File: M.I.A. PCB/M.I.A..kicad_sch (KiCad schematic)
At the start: 44 parts, among them J1 USB_C_Receptacle_USB2.0_16P, SW1 SW_Push, SW2 SW_Push, U1 W25Q128JVS, U2 RP2350B-QFN80, Y1 ABM8-272-T3

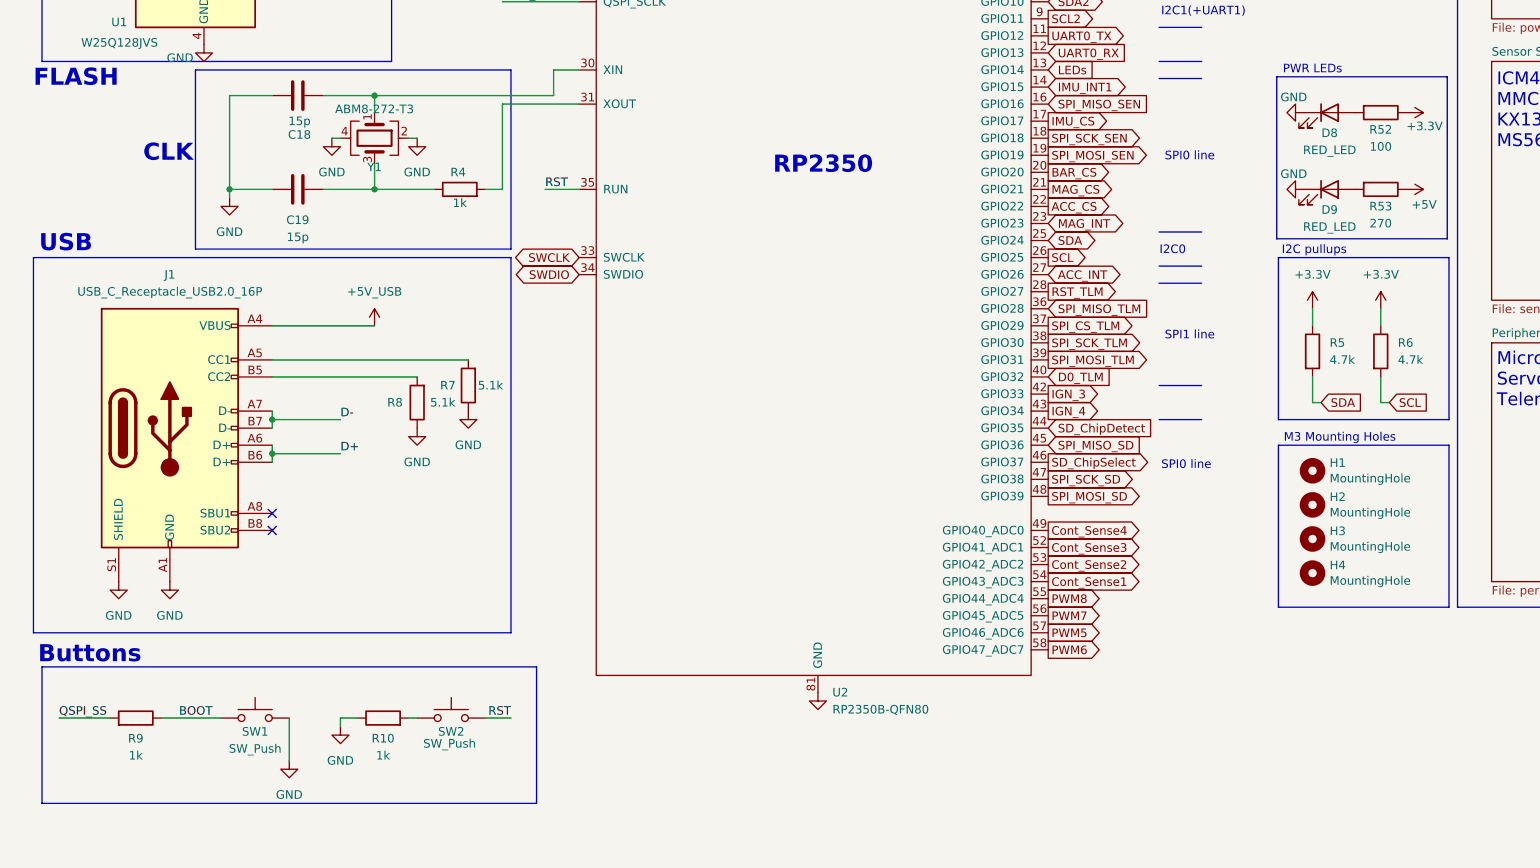
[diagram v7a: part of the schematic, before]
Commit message: Updated top connectors to be TLM_SPI
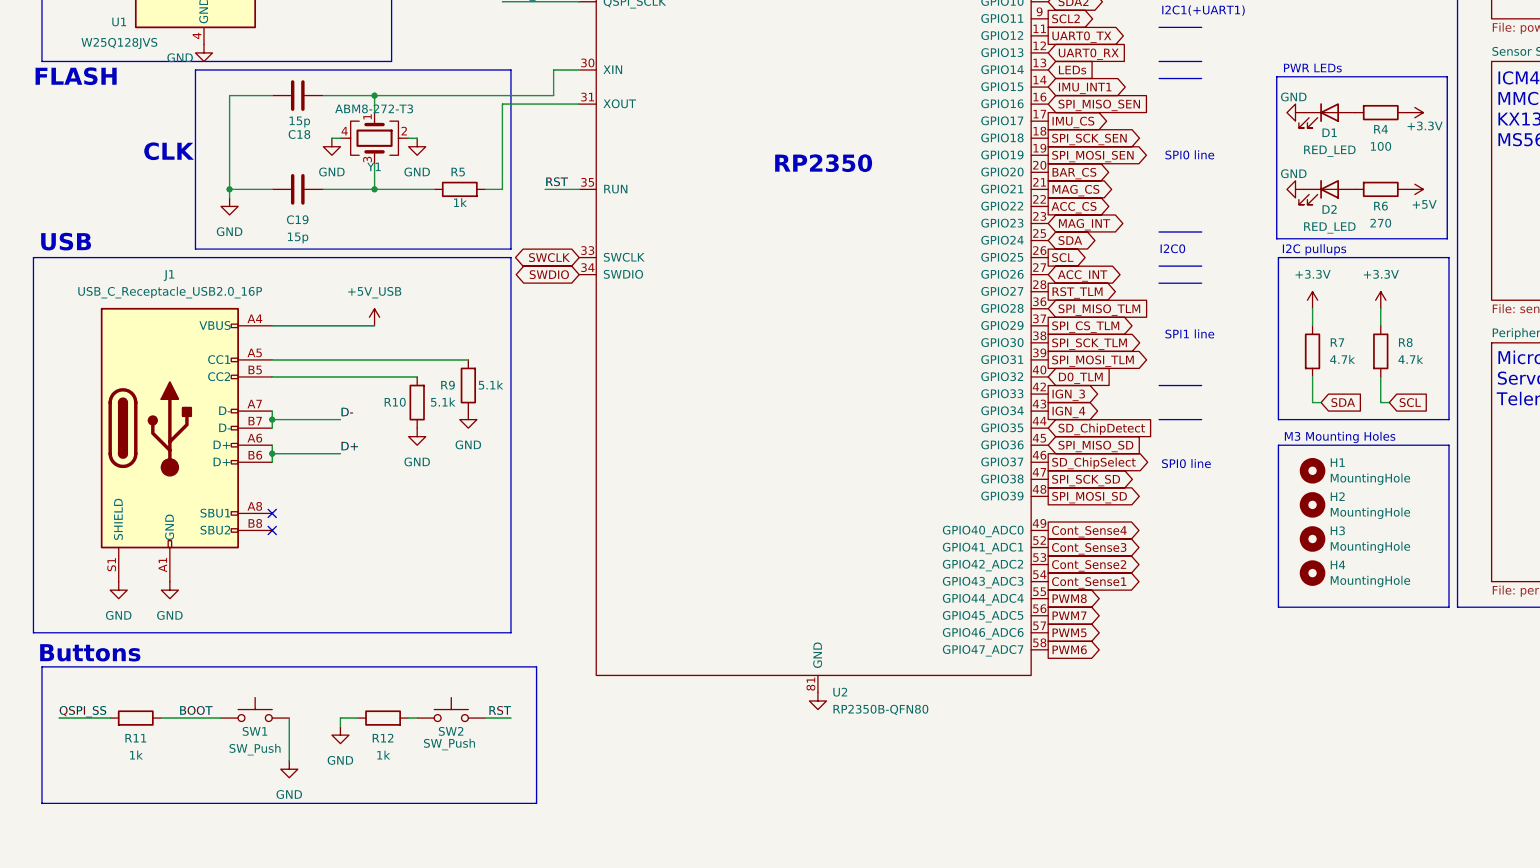
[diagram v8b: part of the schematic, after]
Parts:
- renumbered D8 to D1, D9 to D2, R8 to R10, R9 to R11, R10 to R12, R52 to R4, R4 to R5, R53 to R6, R5 to R7, R6 to R8, R7 to R9
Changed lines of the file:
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@@
 		(on_board yes)
 		(dnp no)
-		(property "Reference" "#PWR0175"
+		(property "Reference" "#PWR015"
 			(at 215.9 91.44 0)
 			(effects
@@
 			(project "M.I.A."
 				(path "/4d55825e-4251-44bf-9376-9abd9228f348"
-					(reference "#PWR0175")
+					(reference "#PWR015")
 					(unit 1)
 				)
@@
 		(dnp no)
 		(fields_autoplaced yes)
-		(property "Reference" "#PWR015"
+		(property "Reference" "#PWR017"
 			(at 72.39 101.6 0)
 			(effects
@@
 			(project "M.I.A."
 				(path "/4d55825e-4251-44bf-9376-9abd9228f348"
-					(reference "#PWR015")
+					(reference "#PWR017")
 					(unit 1)
 				)
@@
 		(on_board yes)
 		(dnp no)
-		(property "Reference" "R52"
+		(property "Reference" "R4"
 			(at 215.9 93.98 90)
 			(effects
@@
 			(project "M.I.A."
 				(path "/4d55825e-4251-44bf-9376-9abd9228f348"
-					(reference "R52")
+					(reference "R4")
 					(unit 1)
 				)
@@
 		(on_board yes)
 		(dnp no)
-		(property "Reference" "R4"
+		(property "Reference" "R5"
 			(at 78.486 100.33 90)
 			(effects
@@
 			(project "M.I.A."
 				(path "/4d55825e-4251-44bf-9376-9abd9228f348"
-					(reference "R4")
+					(reference "R5")
 					(unit 1)
 				)
@@
 		(on_board yes)
 		(dnp no)
-		(property "Reference" "D8"
+		(property "Reference" "D1"
 			(at 208.28 94.488 0)
 			(effects
@@
 			(project "M.I.A."
 				(path "/4d55825e-4251-44bf-9376-9abd9228f348"
-					(reference "D8")
+					(reference "D1")
 					(unit 1)
 				)
@@
 		(dnp no)
 		(fields_autoplaced yes)
-		(property "Reference" "#PWR025"
+		(property "Reference" "#PWR030"
 			(at 53.34 194.31 0)
 			(effects
@@
 			(project "M.I.A."
 				(path "/4d55825e-4251-44bf-9376-9abd9228f348"
-					(reference "#PWR025")
+					(reference "#PWR030")
 					(unit 1)
 				)
@@
 		(dnp no)
 		(fields_autoplaced yes)
-		(property "Reference" "R5"
+		(property "Reference" "R7"
 			(at 208.28 125.7299 0)
 			(effects
@@
 			(project "M.I.A."
 				(path "/4d55825e-4251-44bf-9376-9abd9228f348"
-					(reference "R5")
+					(reference "R7")
 					(unit 1)
 				)
@@
 		(dnp no)
 		(fields_autoplaced yes)
-		(property "Reference" "#PWR018"
+		(property "Reference" "#PWR022"
 			(at 215.9 124.46 0)
 			(effects
@@
 			(project "M.I.A."
 				(path "/4d55825e-4251-44bf-9376-9abd9228f348"
-					(reference "#PWR018")
+					(reference "#PWR022")
 					(unit 1)
 				)
@@
 		(dnp no)
 		(fields_autoplaced yes)
-		(property "Reference" "#PWR020"
+		(property "Reference" "#PWR024"
 			(at 80.01 142.24 0)
 			(effects
@@
 			(project "M.I.A."
 				(path "/4d55825e-4251-44bf-9376-9abd9228f348"
-					(reference "#PWR020")
+					(reference "#PWR024")
 					(unit 1)
 				)
@@
 		(dnp no)
 		(fields_autoplaced yes)
-		(property "Reference" "#PWR016"
+		(property "Reference" "#PWR020"
 			(at 44.45 110.49 0)
 			(effects
@@
 			(project "M.I.A."
 				(path "/4d55825e-4251-44bf-9376-9abd9228f348"
-					(reference "#PWR016")
+					(reference "#PWR020")
 					(unit 1)
 				)
@@
 		(on_board yes)
 		(dnp no)
-		(property "Reference" "R9"
+		(property "Reference" "R11"
 			(at 30.48 184.658 90)
 			(effects
@@
 			(project "M.I.A."
 				(path "/4d55825e-4251-44bf-9376-9abd9228f348"
-					(reference "R9")
+					(reference "R11")
 					(unit 1)
 				)
@@
 		(on_board yes)
 		(dnp no)
-		(property "Reference" "#PWR0172"
+		(property "Reference" "#PWR019"
 			(at 215.9 102.87 0)
 			(effects
@@
 			(project "M.I.A."
 				(path "/4d55825e-4251-44bf-9376-9abd9228f348"
-					(reference "#PWR0172")
+					(reference "#PWR019")
 					(unit 1)
 				)
@@
 		(dnp no)
 		(fields_autoplaced yes)
-		(property "Reference" "R6"
+		(property "Reference" "R8"
 			(at 218.44 125.7299 0)
 			(effects
@@
 			(project "M.I.A."
 				(path "/4d55825e-4251-44bf-9376-9abd9228f348"
-					(reference "R6")
+					(reference "R8")
 					(unit 1)
 				)
@@
 		(dnp no)
 		(fields_autoplaced yes)
-		(property "Reference" "#PWR023"
+		(property "Reference" "#PWR027"
 			(at 35.56 167.64 0)
 			(effects
@@
 			(project "M.I.A."
 				(path "/4d55825e-4251-44bf-9376-9abd9228f348"
-					(reference "#PWR023")
+					(reference "#PWR027")
 					(unit 1)
 				)
@@
 		(on_board yes)
 		(dnp no)
-		(property "Reference" "R53"
+		(property "Reference" "R6"
 			(at 215.9 105.41 90)
 			(effects
@@
 			(project "M.I.A."
 				(path "/4d55825e-4251-44bf-9376-9abd9228f348"
-					(reference "R53")
+					(reference "R6")
 					(unit 1)
 				)
@@
 		(on_board yes)
 		(dnp no)
-		(property "Reference" "R8"
+		(property "Reference" "R10"
 			(at 69.088 134.62 0)
 			(effects
@@
 			(project "M.I.A."
 				(path "/4d55825e-4251-44bf-9376-9abd9228f348"
-					(reference "R8")
+					(reference "R10")
 					(unit 1)
 				)
@@
 		(dnp no)
 		(fields_autoplaced yes)
-		(property "Reference" "#PWR014"
+		(property "Reference" "#PWR016"
 			(at 59.69 101.6 0)
 			(effects
@@
 			(project "M.I.A."
 				(path "/4d55825e-4251-44bf-9376-9abd9228f348"
-					(reference "#PWR014")
+					(reference "#PWR016")
 					(unit 1)
 				)
@@
 		(on_board yes)
 		(dnp no)
-		(property "Reference" "R10"
+		(property "Reference" "R12"
 			(at 67.31 184.658 90)
 			(effects
@@
 			(project "M.I.A."
 				(path "/4d55825e-4251-44bf-9376-9abd9228f348"
-					(reference "R10")
+					(reference "R12")
 					(unit 1)
 				)
@@
 		(on_board yes)
 		(dnp no)
-		(property "Reference" "#PWR0174"
+		(property "Reference" "#PWR014"
 			(at 198.12 91.44 0)
 			(effects
@@
 			(project "M.I.A."
 				(path "/4d55825e-4251-44bf-9376-9abd9228f348"
-					(reference "#PWR0174")
+					(reference "#PWR014")
 					(unit 1)
 				)
@@
 		(dnp no)
 		(fields_autoplaced yes)
-		(property "Reference" "#PWR0150"
+		(property "Reference" "#PWR028"
 			(at 132.08 184.15 0)
 			(effects
@@
 			(project "M.I.A."
 				(path "/4d55825e-4251-44bf-9376-9abd9228f348"
-					(reference "#PWR0150")
+					(reference "#PWR028")
 					(unit 1)
 				)
@@
 		(on_board yes)
 		(dnp no)
-		(property "Reference" "D9"
+		(property "Reference" "D2"
 			(at 208.28 105.918 0)
 			(effects
@@
 			(project "M.I.A."
 				(path "/4d55825e-4251-44bf-9376-9abd9228f348"
-					(reference "D9")
+					(reference "D2")
 					(unit 1)
 				)
@@
 		(on_board yes)
 		(dnp no)
-		(property "Reference" "#PWR0173"
+		(property "Reference" "#PWR018"
 			(at 198.12 102.87 0)
 			(effects
@@
 			(project "M.I.A."
 				(path "/4d55825e-4251-44bf-9376-9abd9228f348"
-					(reference "#PWR0173")
+					(reference "#PWR018")
 					(unit 1)
 				)
@@
 		(dnp no)
 		(fields_autoplaced yes)
-		(property "Reference" "#PWR021"
+		(property "Reference" "#PWR025"
 			(at 72.39 144.78 0)
 			(effects
@@
 			(project "M.I.A."
 				(path "/4d55825e-4251-44bf-9376-9abd9228f348"
-					(reference "#PWR021")
+					(reference "#PWR025")
 					(unit 1)
 				)
@@
 		(dnp no)
 		(fields_autoplaced yes)
-		(property "Reference" "#PWR024"
+		(property "Reference" "#PWR029"
 			(at 60.96 189.23 0)
 			(effects
@@
 			(project "M.I.A."
 				(path "/4d55825e-4251-44bf-9376-9abd9228f348"
-					(reference "#PWR024")
+					(reference "#PWR029")
 					(unit 1)
 				)
@@
 		(dnp no)
 		(fields_autoplaced yes)
-		(property "Reference" "#PWR019"
+		(property "Reference" "#PWR023"
 			(at 66.04 127 0)
 			(effects
@@
 			(project ""
 				(path "/4d55825e-4251-44bf-9376-9abd9228f348"
-					(reference "#PWR019")
+					(reference "#PWR023")
 					(unit 1)
 				)
@@
 		(dnp no)
 		(fields_autoplaced yes)
-		(property "Reference" "#PWR022"
+		(property "Reference" "#PWR026"
 			(at 27.94 167.64 0)
 			(effects
@@
 			(project "M.I.A."
 				(path "/4d55825e-4251-44bf-9376-9abd9228f348"
-					(reference "#PWR022")
+					(reference "#PWR026")
 					(unit 1)
 				)
@@
 		(on_board yes)
 		(dnp no)
-		(property "Reference" "R7"
+		(property "Reference" "R9"
 			(at 76.962 132.08 0)
 			(effects
@@
 			(project "M.I.A."
 				(path "/4d55825e-4251-44bf-9376-9abd9228f348"
-					(reference "R7")
+					(reference "R9")
 					(unit 1)
 				)
@@
 		(on_board yes)
 		(dnp no)
-		(property "Reference" "#PWR017"
+		(property "Reference" "#PWR021"
 			(at 205.74 124.46 0)
 			(effects
@@
 			(project "M.I.A."
 				(path "/4d55825e-4251-44bf-9376-9abd9228f348"
-					(reference "#PWR017")
+					(reference "#PWR021")
 					(unit 1)
 				)
